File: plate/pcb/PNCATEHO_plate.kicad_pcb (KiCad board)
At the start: 2 copper layers, 93.5 x 54.1 mm, 10 parts, among them SW1 SW_PUSH, SW10 SW_PUSH, SW2 SW_PUSH, SW3 SW_PUSH, SW4 SW_PUSH, SW5 SW_PUSH, SW6 SW_PUSH, SW7 SW_PUSH, SW8 SW_PUSH, SW9 SW_PUSH

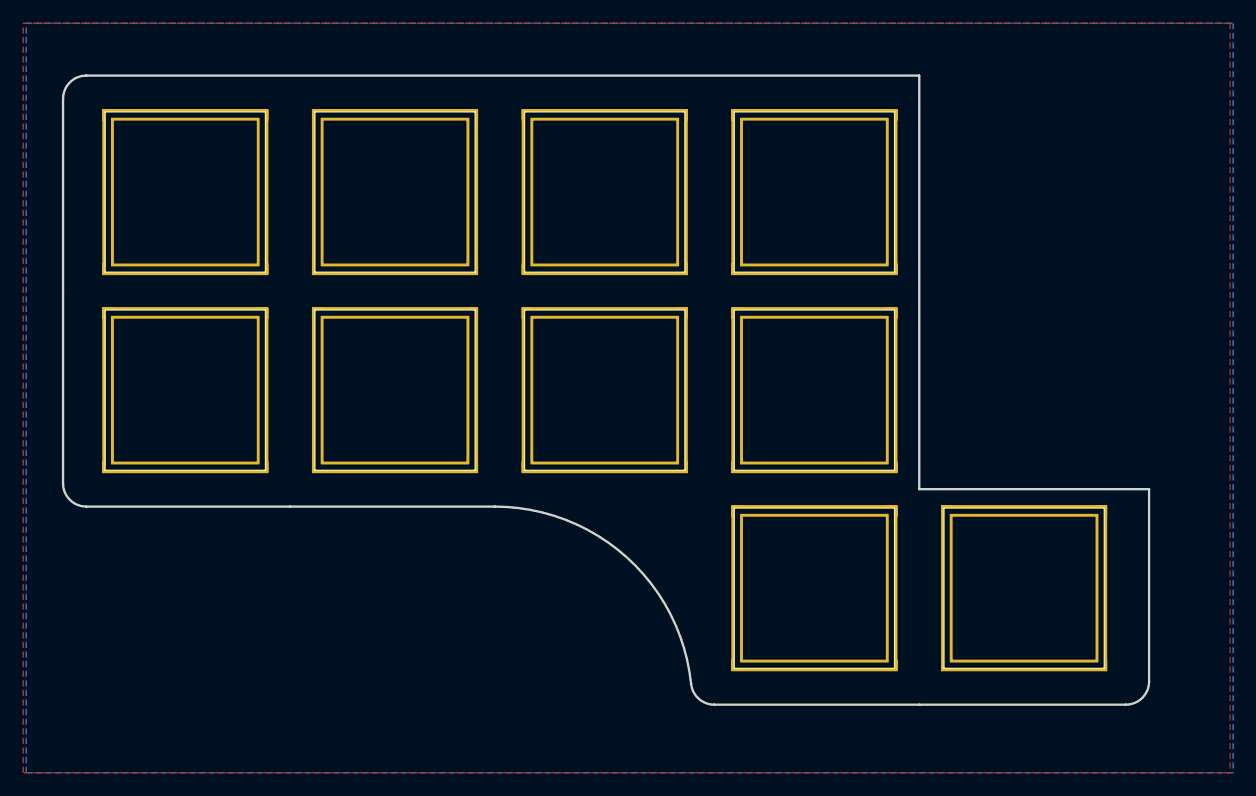
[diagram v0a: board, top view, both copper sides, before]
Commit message: v3
* Power switch for wireless controllers(optional)
* Two halves inscribed in 100x100 mm(optional)
* Three mounting screws
* One PCB for right and left versions
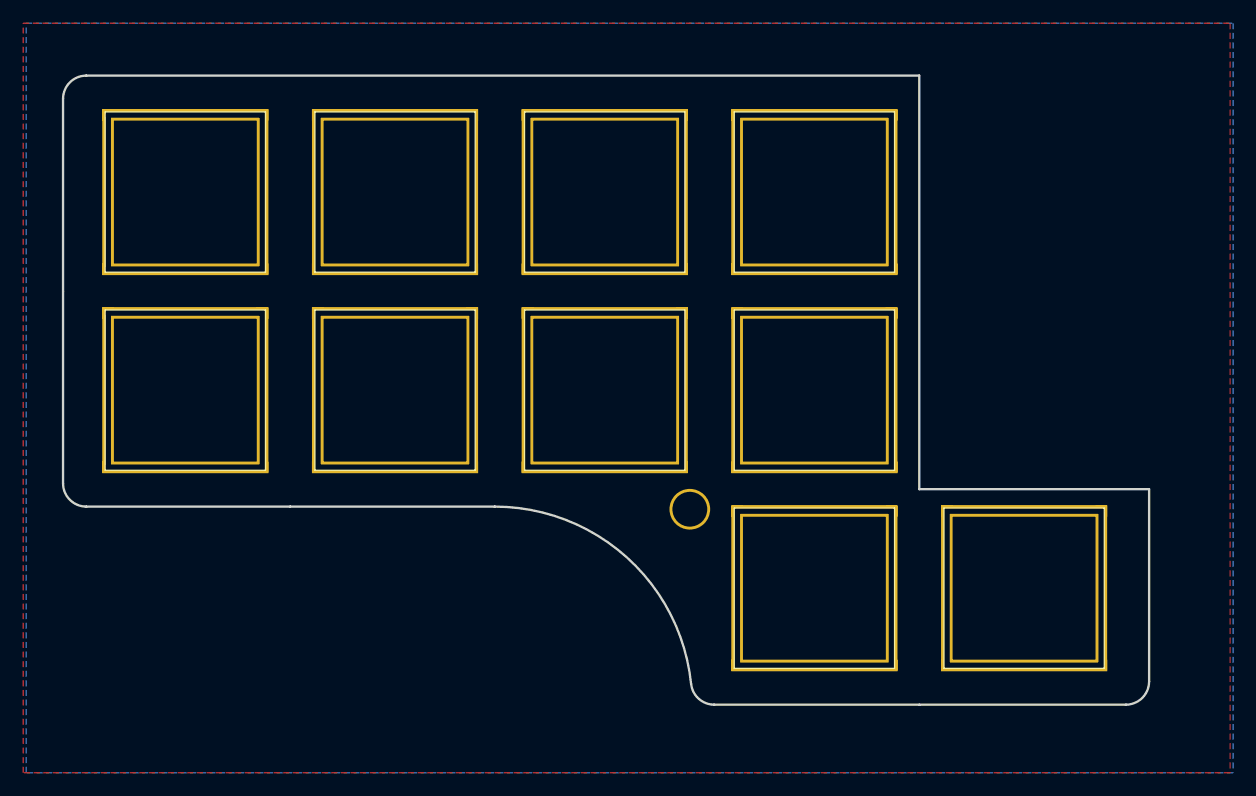
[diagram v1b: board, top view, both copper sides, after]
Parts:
- added ?: , , F.Cu at (82.3, 64.9)
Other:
- net class Default removed
- rule pad_to_mask_clearance: 0.051 -> 0
